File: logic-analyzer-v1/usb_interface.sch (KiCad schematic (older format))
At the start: 21 parts

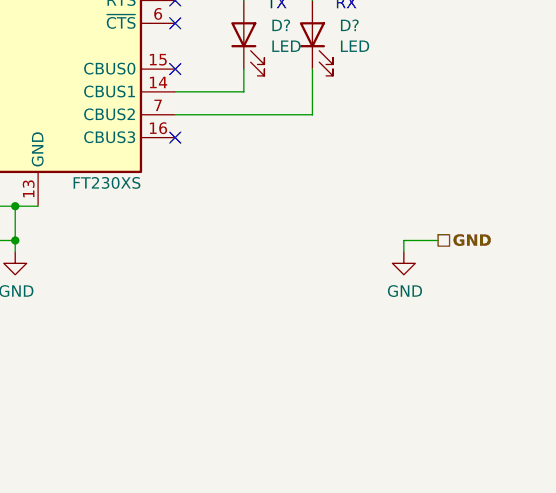
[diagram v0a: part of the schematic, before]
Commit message: changing sram blocks from new library
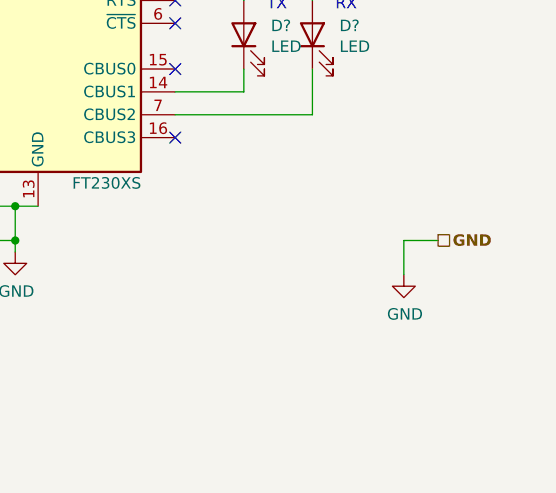
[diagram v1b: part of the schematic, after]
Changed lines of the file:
@@
 L power:GND #PWR?
 U 1 1 5F0C0B43
-P 9750 4650
-F 0 "#PWR?" H 9750 4400 50  0001 C CNN
-F 1 "GND" H 9755 4477 50  0000 C CNN
-F 2 "" H 9750 4650 50  0001 C CNN
-F 3 "" H 9750 4650 50  0001 C CNN
-	1    9750 4650
+P 9750 4750
+F 0 "#PWR?" H 9750 4500 50  0001 C CNN
+F 1 "GND" H 9755 4577 50  0000 C CNN
+F 2 "" H 9750 4750 50  0001 C CNN
+F 3 "" H 9750 4750 50  0001 C CNN
+	1    9750 4750
 	1    0    0    -1
 $EndComp
 Wire Wire Line
-	9750 4650 9750 4600
+	9750 4750 9750 4600
 Wire Wire Line
 	9750 4600 9900 4600
